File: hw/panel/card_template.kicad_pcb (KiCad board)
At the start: 2 copper layers, 48 x 75 mm, 1 part, among them J1 SLOT

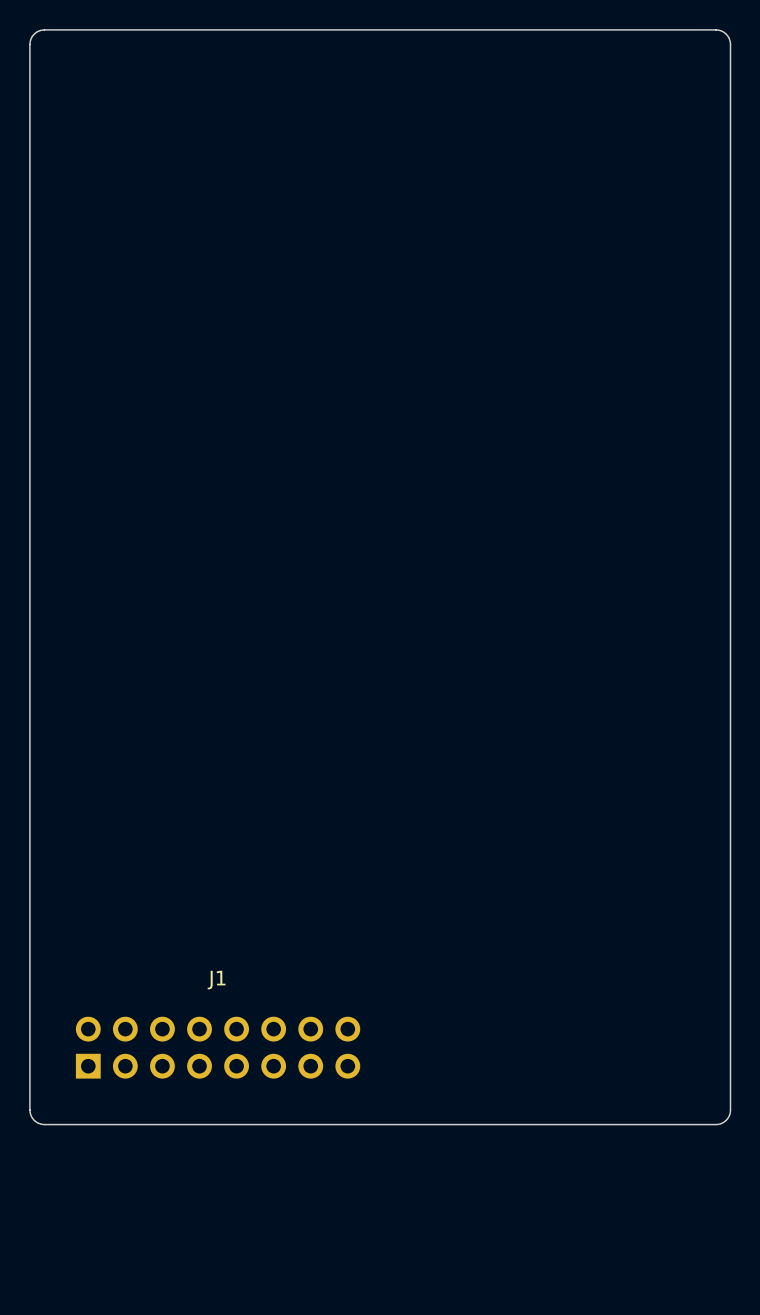
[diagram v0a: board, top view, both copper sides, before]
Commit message: hw/panel: cassette, rails and backplane at 80 mm
Each section becomes a cassette: segment, rails, four M3 standoffs sized
to its deepest socket, and a full-height card with a 2x5 ribbon header on
its back. The backplane, 80 mm behind the plate, carries one SNAC port
per slot as a USB3-A socket and a ribbon header in parallel, the button
and display harness header, and four hub headers for USB sections. The
2x8 slot header and the horizontal main board are gone. The port pinout
is 2x5: 5 V, ground, seven IO lines in SNAC channel order.

gen_panel.py now writes backplane.kicad_pcb with placeholder USB3-A
footprints and shrouded header footprints; the card template gets the
standoff holes and the ribbon header. README rewritten for the card cage.

Co-Authored-By: Claude Fable 5.1 <noreply@anthropic.com>
Claude-Session: https://claude.ai/code/session_01F2VQWGQ7N9EUTJecPe9sTD
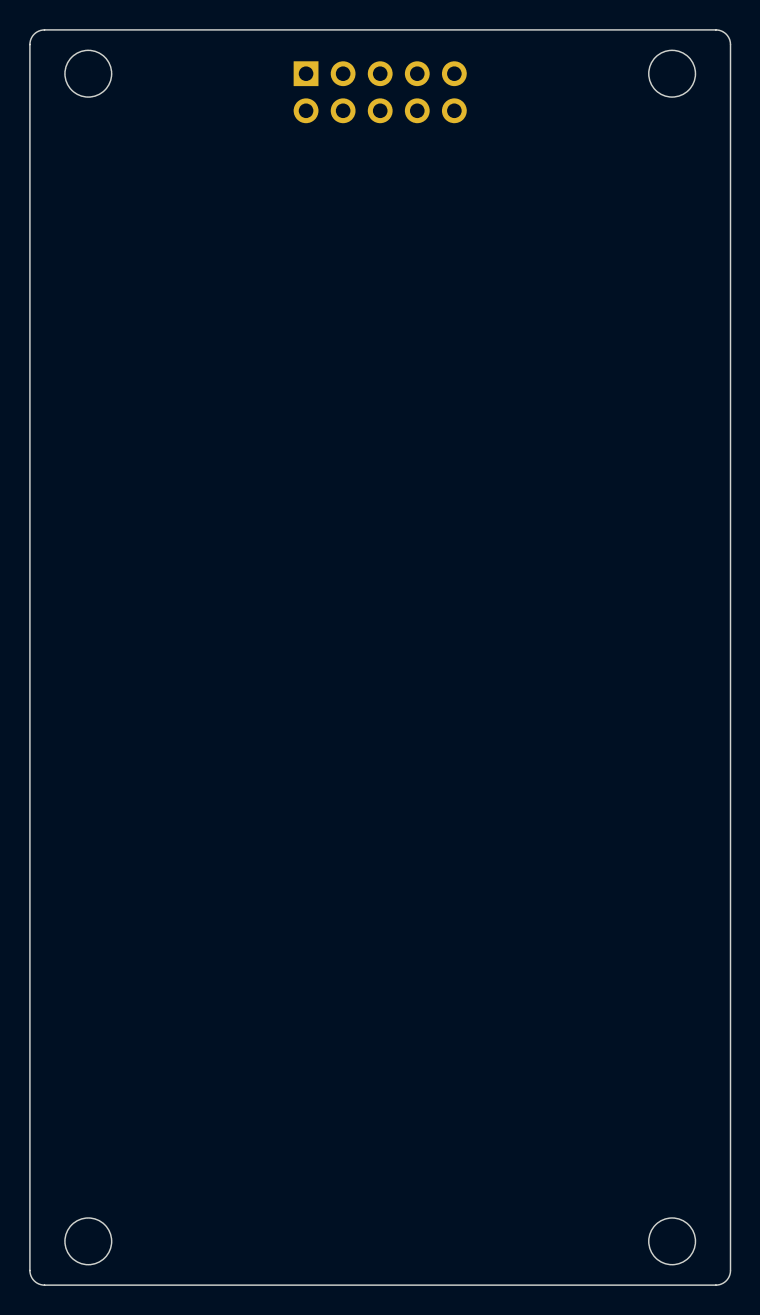
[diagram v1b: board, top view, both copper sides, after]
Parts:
- J1: value SLOT -> RIBBON; footprint panel:PinHeader_2x08_P2.54mm_Horizontal_Edge -> panel:BoxHeader_5x02_P2.54mm; moved to B.Cu
- moved J1 69.6 mm to (18.9, 3.00)
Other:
- board size 48 x 75 mm -> 48 x 86 mm
- board text added: "J1 on the back face: 2x5 box header, ribbon to the backplane; pin 1 = +5V (README)"
- board text added: "corner holes: M3 standoffs to the rails, length = deepest socket on this card"
- board text removed: "J1 pin 1 = +5V (README, slot pinout); header sits in the module's leftmost slot"
- board text removed: "bottom edge rests on the main board; J1 pins exit downward into the slot's 2x8 socket"
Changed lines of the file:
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@@
   (general (thickness 1.6) (legacy_teardrops no))
   (paper "A3")
-  (title_block (title "module card template (2 slot, parallel to the plate, viewed from the front)") (comment 1 "generated by hw/panel/gen_panel.py - do not edit by hand"))
+  (title_block (title "cassette card template (2 slot, parallel to the plate, viewed from the front)") (comment 1 "generated by hw/panel/gen_panel.py - do not edit by hand"))
   (layers
     (0 "F.Cu" signal)
@@
   (gr_line (start 1 0) (end 47 0) (stroke (width 0.1) (type default)) (layer "Edge.Cuts"))
   (gr_arc (start 47 0) (mid 47.707 0.293) (end 48 1) (stroke (width 0.1) (type default)) (layer "Edge.Cuts"))
-  (gr_line (start 48 1) (end 48 74) (stroke (width 0.1) (type default)) (layer "Edge.Cuts"))
-  (gr_arc (start 48 74) (mid 47.707 74.707) (end 47 75) (stroke (width 0.1) (type default)) (layer "Edge.Cuts"))
-  (gr_line (start 47 75) (end 1 75) (stroke (width 0.1) (type default)) (layer "Edge.Cuts"))
-  (gr_arc (start 1 75) (mid 0.293 74.707) (end 0 74) (stroke (width 0.1) (type default)) (layer "Edge.Cuts"))
-  (gr_line (start 0 74) (end 0 1) (stroke (width 0.1) (type default)) (layer "Edge.Cuts"))
+  (gr_line (start 48 1) (end 48 85) (stroke (width 0.1) (type default)) (layer "Edge.Cuts"))
+  (gr_arc (start 48 85) (mid 47.707 85.707) (end 47 86) (stroke (width 0.1) (type default)) (layer "Edge.Cuts"))
+  (gr_line (start 47 86) (end 1 86) (stroke (width 0.1) (type default)) (layer "Edge.Cuts"))
+  (gr_arc (start 1 86) (mid 0.293 85.707) (end 0 85) (stroke (width 0.1) (type default)) (layer "Edge.Cuts"))
+  (gr_line (start 0 85) (end 0 1) (stroke (width 0.1) (type default)) (layer "Edge.Cuts"))
   (gr_arc (start 0 1) (mid 0.293 0.293) (end 1 0) (stroke (width 0.1) (type default)) (layer "Edge.Cuts"))
-  (gr_line (start 0 8) (end 48 8) (stroke (width 0.1) (type default)) (layer "Cmts.User"))
-  (gr_text "row 1 centre (panel y 17)" (at 2 6.8 0) (layer "Cmts.User") (effects (font (size 1.0 1.0) (thickness 0.15)) (justify left)))
-  (gr_line (start 0 26) (end 48 26) (stroke (width 0.1) (type default)) (layer "Cmts.User"))
-  (gr_text "row 2 centre (panel y 35)" (at 2 24.8 0) (layer "Cmts.User") (effects (font (size 1.0 1.0) (thickness 0.15)) (justify left)))
-  (gr_line (start 0 44) (end 48 44) (stroke (width 0.1) (type default)) (layer "Cmts.User"))
-  (gr_text "row 3 centre (panel y 53)" (at 2 42.8 0) (layer "Cmts.User") (effects (font (size 1.0 1.0) (thickness 0.15)) (justify left)))
-  (gr_line (start 0 62) (end 48 62) (stroke (width 0.1) (type default)) (layer "Cmts.User"))
-  (gr_text "row 4 centre (panel y 71)" (at 2 60.8 0) (layer "Cmts.User") (effects (font (size 1.0 1.0) (thickness 0.15)) (justify left)))
-  (gr_line (start 24 0) (end 24 75) (stroke (width 0.1) (type default)) (layer "Cmts.User"))
+  (gr_circle (center 4 3) (end 5.6 3) (stroke (width 0.1) (type default)) (fill none) (layer "Edge.Cuts"))
+  (gr_circle (center 44 3) (end 45.6 3) (stroke (width 0.1) (type default)) (fill none) (layer "Edge.Cuts"))
+  (gr_circle (center 4 83) (end 5.6 83) (stroke (width 0.1) (type default)) (fill none) (layer "Edge.Cuts"))
+  (gr_circle (center 44 83) (end 45.6 83) (stroke (width 0.1) (type default)) (fill none) (layer "Edge.Cuts"))
+  (gr_line (start 0 16) (end 48 16) (stroke (width 0.1) (type default)) (layer "Cmts.User"))
+  (gr_text "row 1 centre (panel y 17)" (at 2 14.8 0) (layer "Cmts.User") (effects (font (size 1.0 1.0) (thickness 0.15)) (justify left)))
+  (gr_line (start 0 34) (end 48 34) (stroke (width 0.1) (type default)) (layer "Cmts.User"))
+  (gr_text "row 2 centre (panel y 35)" (at 2 32.8 0) (layer "Cmts.User") (effects (font (size 1.0 1.0) (thickness 0.15)) (justify left)))
+  (gr_line (start 0 52) (end 48 52) (stroke (width 0.1) (type default)) (layer "Cmts.User"))
+  (gr_text "row 3 centre (panel y 53)" (at 2 50.8 0) (layer "Cmts.User") (effects (font (size 1.0 1.0) (thickness 0.15)) (justify left)))
+  (gr_line (start 0 70) (end 48 70) (stroke (width 0.1) (type default)) (layer "Cmts.User"))
+  (gr_text "row 4 centre (panel y 71)" (at 2 68.8 0) (layer "Cmts.User") (effects (font (size 1.0 1.0) (thickness 0.15)) (justify left)))
+  (gr_line (start 24 0) (end 24 86) (stroke (width 0.1) (type default)) (layer "Cmts.User"))
   (gr_text "slot boundary" (at 24 -1.5 0) (layer "Cmts.User") (effects (font (size 0.9 0.9) (thickness 0.135))))
-  (footprint "panel:PinHeader_2x08_P2.54mm_Horizontal_Edge" (layer "F.Cu") (at 4 71)
-    (property "Reference" "J1" (at 8.89 -6 0) (layer "F.SilkS") (effects (font (size 1 1) (thickness 0.15))))
-    (property "Value" "SLOT" (at 8.89 3 0) (layer "F.Fab") (effects (font (size 1 1) (thickness 0.15))))
+  (footprint "panel:BoxHeader_5x02_P2.54mm" (layer "B.Cu") (at 18.92 3 0)
+    (property "Reference" "J1" (at 5.08 -4.68 0) (layer "B.SilkS") (effects (font (size 1 1) (thickness 0.15))))
+    (property "Value" "RIBBON" (at 0 3 0) (layer "B.Fab") (effects (font (size 1 1) (thickness 0.15))))
     (attr through_hole)
-    (fp_rect (start -1.27 -3.81) (end 19.05 1.27) (stroke (width 0.1) (type default)) (fill none) (layer "F.Fab"))
+    (fp_rect (start -2.52 -3.18) (end 12.68 5.72) (stroke (width 0.1) (type default)) (fill none) (layer "B.Fab"))
+    (fp_rect (start 3.08 -3.58) (end 7.08 -3.18) (stroke (width 0.1) (type default)) (fill none) (layer "B.Fab"))
     (pad "1" thru_hole rect (at 0 0) (size 1.7 1.7) (drill 1.0) (layers "*.Cu" "*.Mask") (remove_unused_layers no))
-    (pad "2" thru_hole oval (at 0 -2.54) (size 1.7 1.7) (drill 1.0) (layers "*.Cu" "*.Mask") (remove_unused_layers no))
+    (pad "2" thru_hole oval (at 0 2.54) (size 1.7 1.7) (drill 1.0) (layers "*.Cu" "*.Mask") (remove_unused_layers no))
     (pad "3" thru_hole oval (at 2.54 0) (size 1.7 1.7) (drill 1.0) (layers "*.Cu" "*.Mask") (remove_unused_layers no))
-    (pad "4" thru_hole oval (at 2.54 -2.54) (size 1.7 1.7) (drill 1.0) (layers "*.Cu" "*.Mask") (remove_unused_layers no))
+    (pad "4" thru_hole oval (at 2.54 2.54) (size 1.7 1.7) (drill 1.0) (layers "*.Cu" "*.Mask") (remove_unused_layers no))
     (pad "5" thru_hole oval (at 5.08 0) (size 1.7 1.7) (drill 1.0) (layers "*.Cu" "*.Mask") (remove_unused_layers no))
-    (pad "6" thru_hole oval (at 5.08 -2.54) (size 1.7 1.7) (drill 1.0) (layers "*.Cu" "*.Mask") (remove_unused_layers no))
+    (pad "6" thru_hole oval (at 5.08 2.54) (size 1.7 1.7) (drill 1.0) (layers "*.Cu" "*.Mask") (remove_unused_layers no))
     (pad "7" thru_hole oval (at 7.62 0) (size 1.7 1.7) (drill 1.0) (layers "*.Cu" "*.Mask") (remove_unused_layers no))
-    (pad "8" thru_hole oval (at 7.62 -2.54) (size 1.7 1.7) (drill 1.0) (layers "*.Cu" "*.Mask") (remove_unused_layers no))
+    (pad "8" thru_hole oval (at 7.62 2.54) (size 1.7 1.7) (drill 1.0) (layers "*.Cu" "*.Mask") (remove_unused_layers no))
     (pad "9" thru_hole oval (at 10.16 0) (size 1.7 1.7) (drill 1.0) (layers "*.Cu" "*.Mask") (remove_unused_layers no))
-    (pad "10" thru_hole oval (at 10.16 -2.54) (size 1.7 1.7) (drill 1.0) (layers "*.Cu" "*.Mask") (remove_unused_layers no))
-    (pad "11" thru_hole oval (at 12.7 0) (size 1.7 1.7) (drill 1.0) (layers "*.Cu" "*.Mask") (remove_unused_layers no))
-    (pad "12" thru_hole oval (at 12.7 -2.54) (size 1.7 1.7) (drill 1.0) (layers "*.Cu" "*.Mask") (remove_unused_layers no))
-    (pad "13" thru_hole oval (at 15.24 0) (size 1.7 1.7) (drill 1.0) (layers "*.Cu" "*.Mask") (remove_unused_layers no))
-    (pad "14" thru_hole oval (at 15.24 -2.54) (size 1.7 1.7) (drill 1.0) (layers "*.Cu" "*.Mask") (remove_unused_layers no))
-    (pad "15" thru_hole oval (at 17.78 0) (size 1.7 1.7) (drill 1.0) (layers "*.Cu" "*.Mask") (remove_unused_layers no))
-    (pad "16" thru_hole oval (at 17.78 -2.54) (size 1.7 1.7) (drill 1.0) (layers "*.Cu" "*.Mask") (remove_unused_layers no))
+    (pad "10" thru_hole oval (at 10.16 2.54) (size 1.7 1.7) (drill 1.0) (layers "*.Cu" "*.Mask") (remove_unused_layers no))
   )
   (gr_text "front face: straight sockets here; right-angle sockets on a horizontal shelf sub-board" (at 24 -4 0) (layer "Cmts.User") (effects (font (size 1.2 1.2) (thickness 0.18))))
-  (gr_text "bottom edge rests on the main board; J1 pins exit downward into the slot's 2x8 socket" (at 24 78 0) (layer "Cmts.User") (effects (font (size 1.2 1.2) (thickness 0.18))))
-  (gr_text "J1 pin 1 = +5V (README, slot pinout); header sits in the module's leftmost slot" (at 24 76.5 0) (layer "Cmts.User") (effects (font (size 1.0 1.0) (thickness 0.15)) (justify left)))
+  (gr_text "corner holes: M3 standoffs to the rails, length = deepest socket on this card" (at 24 89 0) (layer "Cmts.User") (effects (font (size 1.2 1.2) (thickness 0.18))))
+  (gr_text "J1 on the back face: 2x5 box header, ribbon to the backplane; pin 1 = +5V (README)" (at 24 11.5 0) (layer "Cmts.User") (effects (font (size 1.0 1.0) (thickness 0.15))))
 )
